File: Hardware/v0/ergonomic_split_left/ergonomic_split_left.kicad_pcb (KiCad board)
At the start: 2 copper layers, 182.6 x 172.4 mm, 96 parts, among them J1 USB_C_Receptacle_USB2.0, J2 Right_Interface, J3 Conn_01x02_Male, J5 Conn_02x03_Odd_Even, SW1 SW_Push, SW10 L31, SW11 L41, SW12 L51, SW13 L02, SW14 L12, SW15 L22, SW16 L32, SW17 L42, SW18 L52, SW19 L03, SW2 L00, SW20 L13, SW21 L23, SW22 L33, SW23 L43, SW24 L53, SW25 L04, SW26 L14, SW27 L24, SW28 L34, SW29 L44, SW3 L10, SW30 L54, SW31 L05, SW32 L15, SW33 L25, SW34 L35, SW35 L55, SW36 L16, SW37 L36, SW38 L56, SW39 L06, SW4 L20, SW40 L_Encoder, SW5 L30, SW6 L40, SW7 L01, SW8 L11, SW9 L21, U1 SRV05-4, U2 PCAL9555AHF, U6 ATmega32U4-AU, U9 TCR2EF33, X2 KC2016K

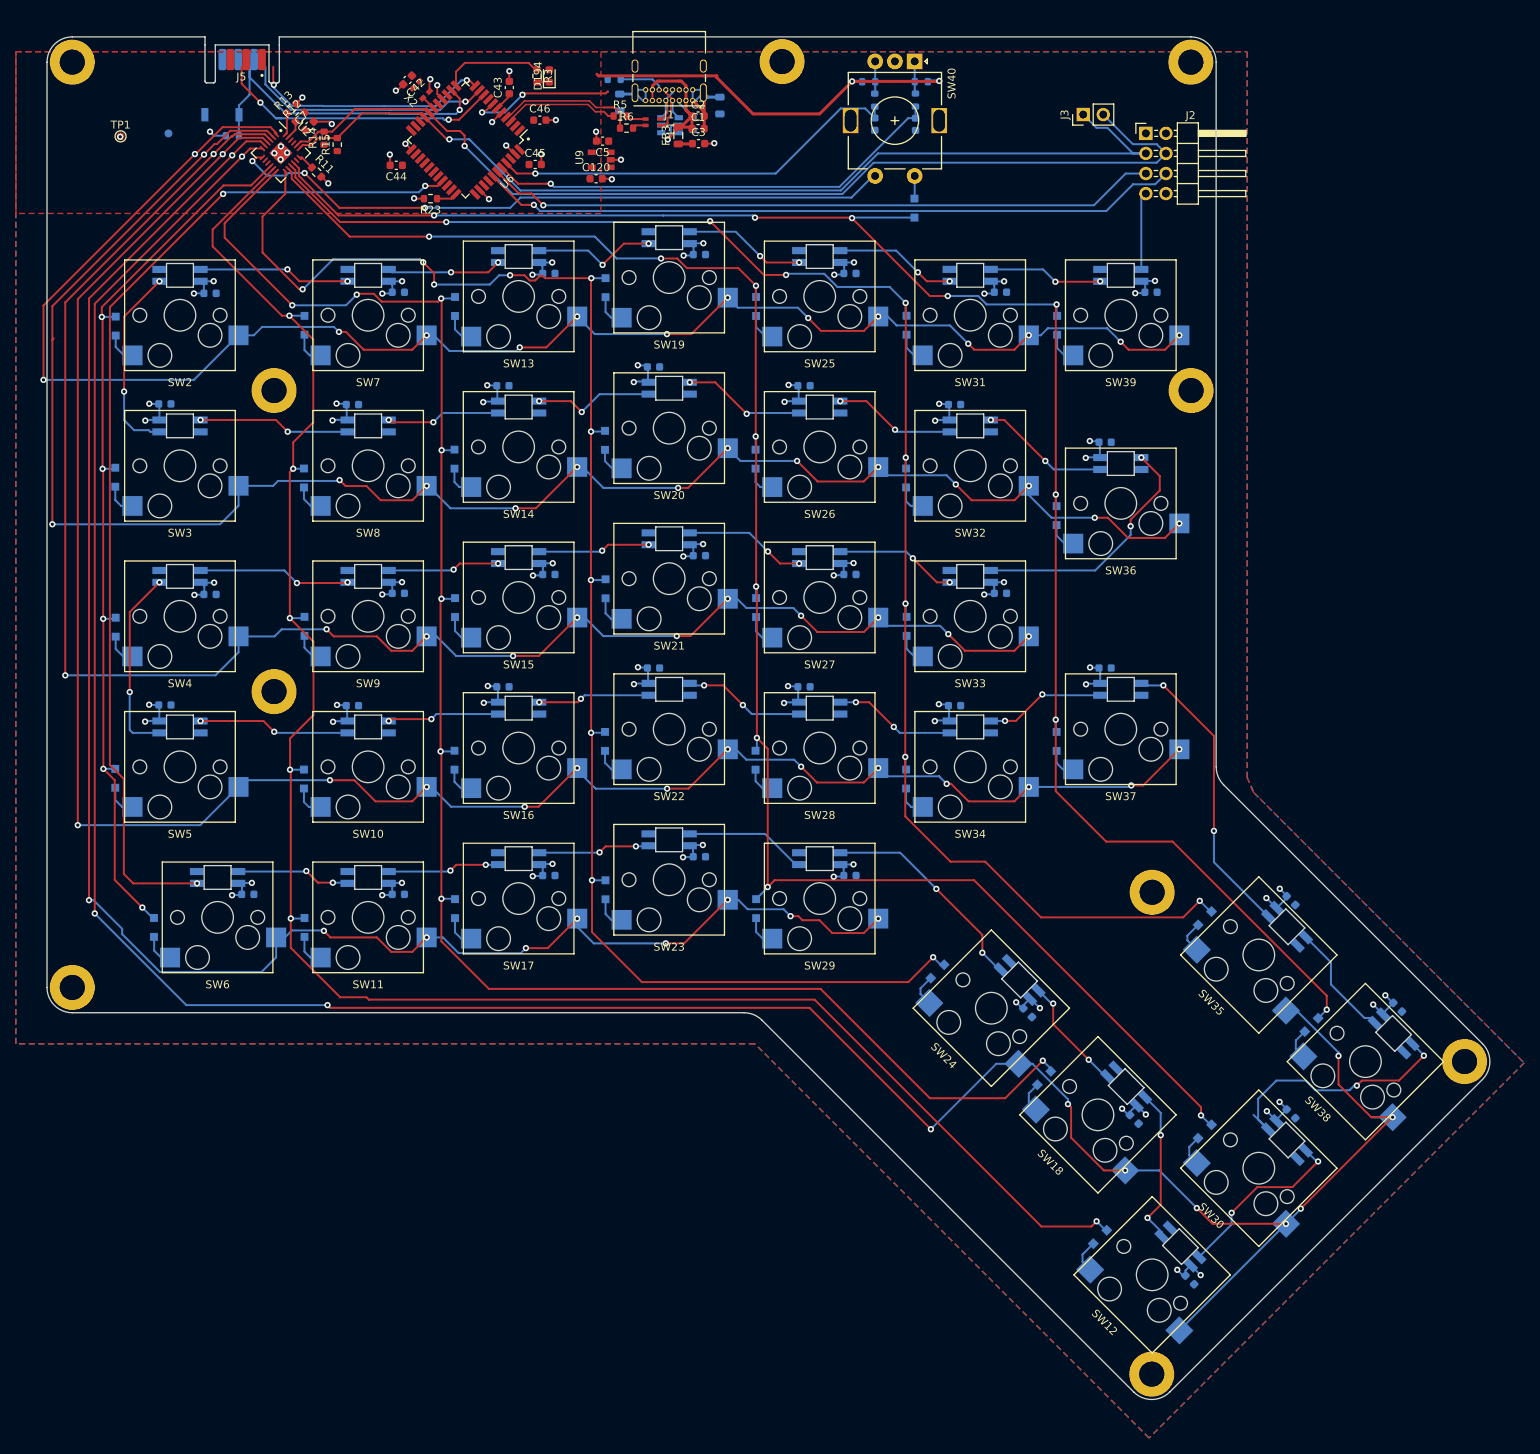
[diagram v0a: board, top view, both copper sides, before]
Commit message: Fixing power planes and connector positions
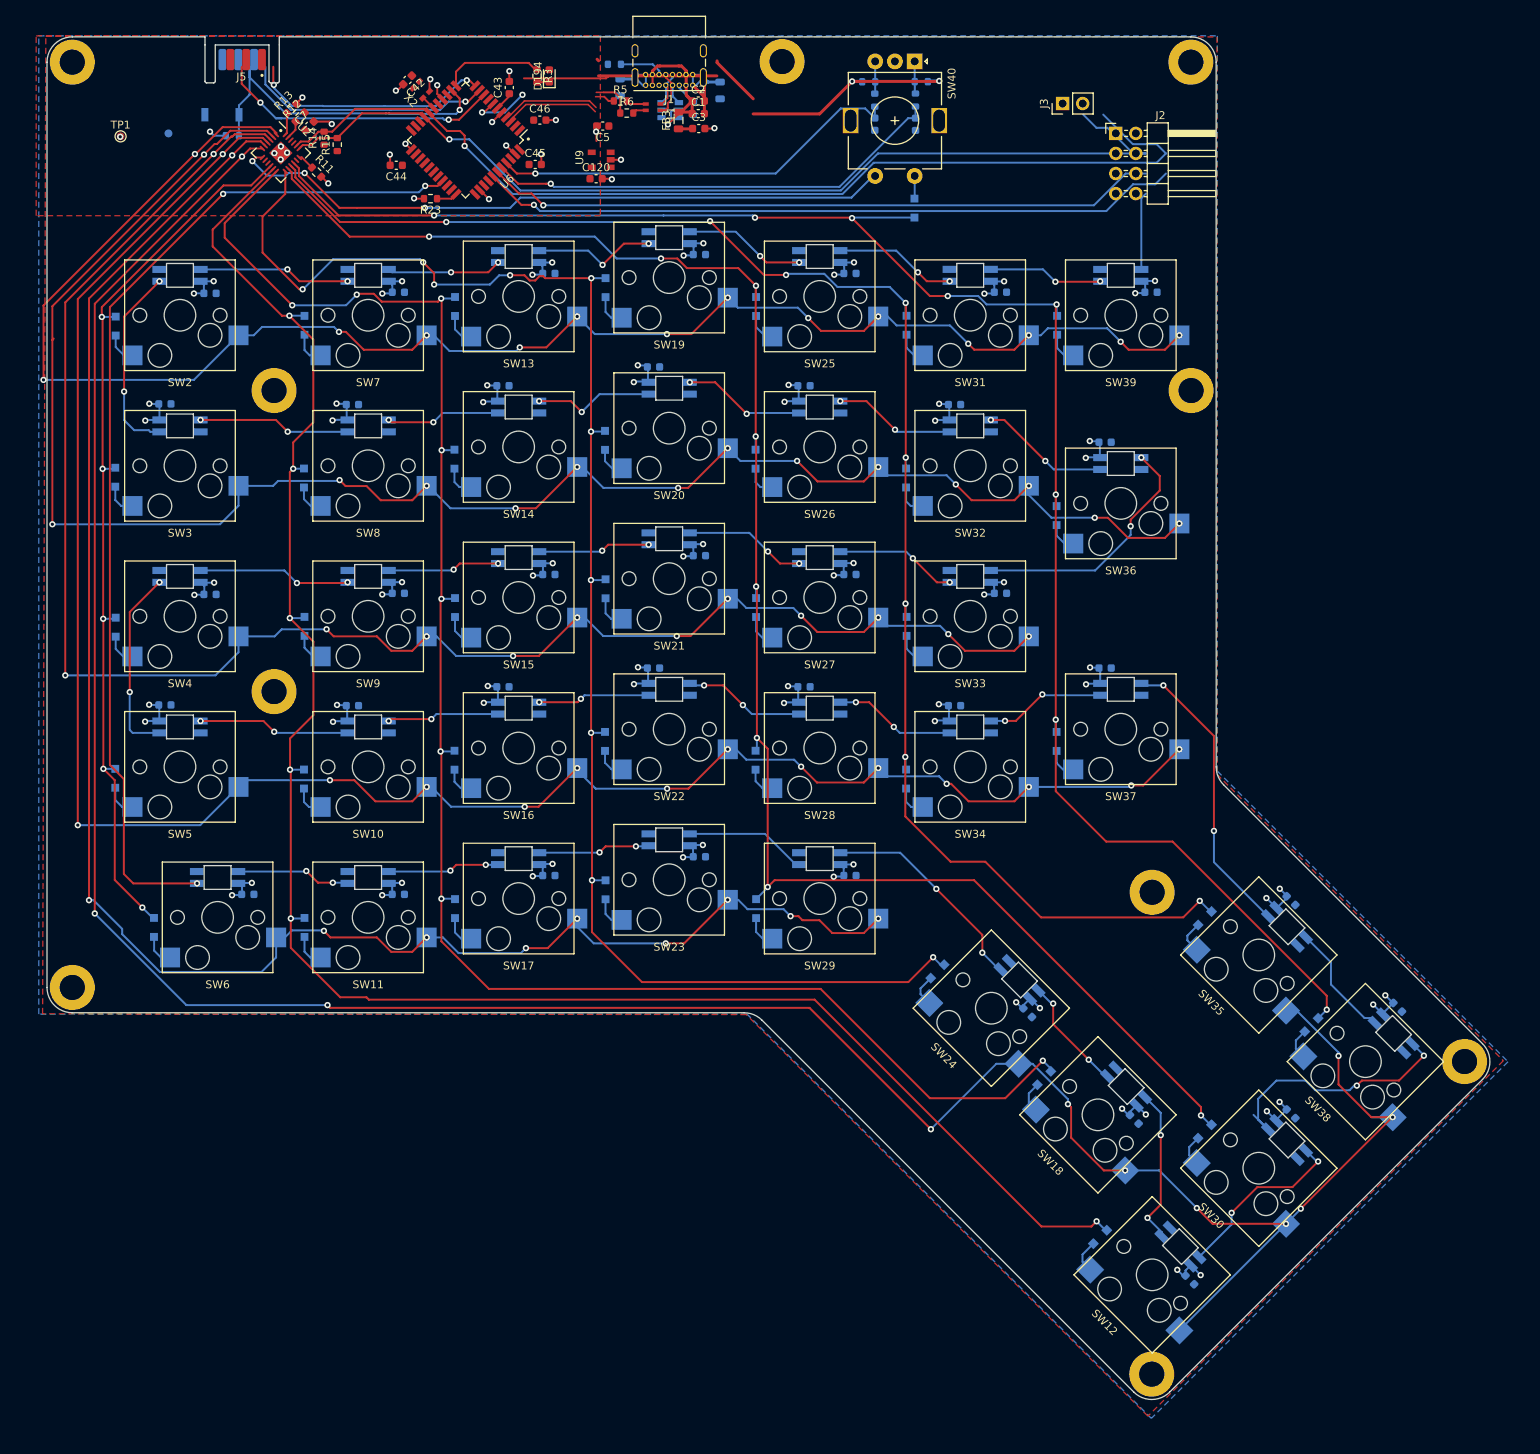
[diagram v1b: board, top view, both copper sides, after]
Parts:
- moved J2 3.81 mm to (212.1, 65.9)
- moved J3 2.95 mm to (205.4, 62.1)
- moved J1 1.93 mm to (158.5, 59.8)
- moved C1 1.91 mm to (159.3, 63.4)
- moved L1 1.91 mm to (153.5, 62.6)
- moved C5 1.91 mm to (147.2, 65.0)
- moved FB3 1.91 mm to (156.8, 64.2)
- moved R1 1.91 mm to (148.6, 57.1)
- moved R6 1.91 mm to (150.2, 63.3)
- moved C3 1.91 mm to (159.3, 65.3)
- moved FB1 1.91 mm to (162.0, 60.5)
- moved FB2 1.91 mm to (149.3, 60.1)
- moved R5 1.91 mm to (149.4, 61.8)
- moved U1 1.91 mm to (155.7, 62.9)
- moved C2 1.91 mm to (159.3, 61.8)
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
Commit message: Cleaning up routing
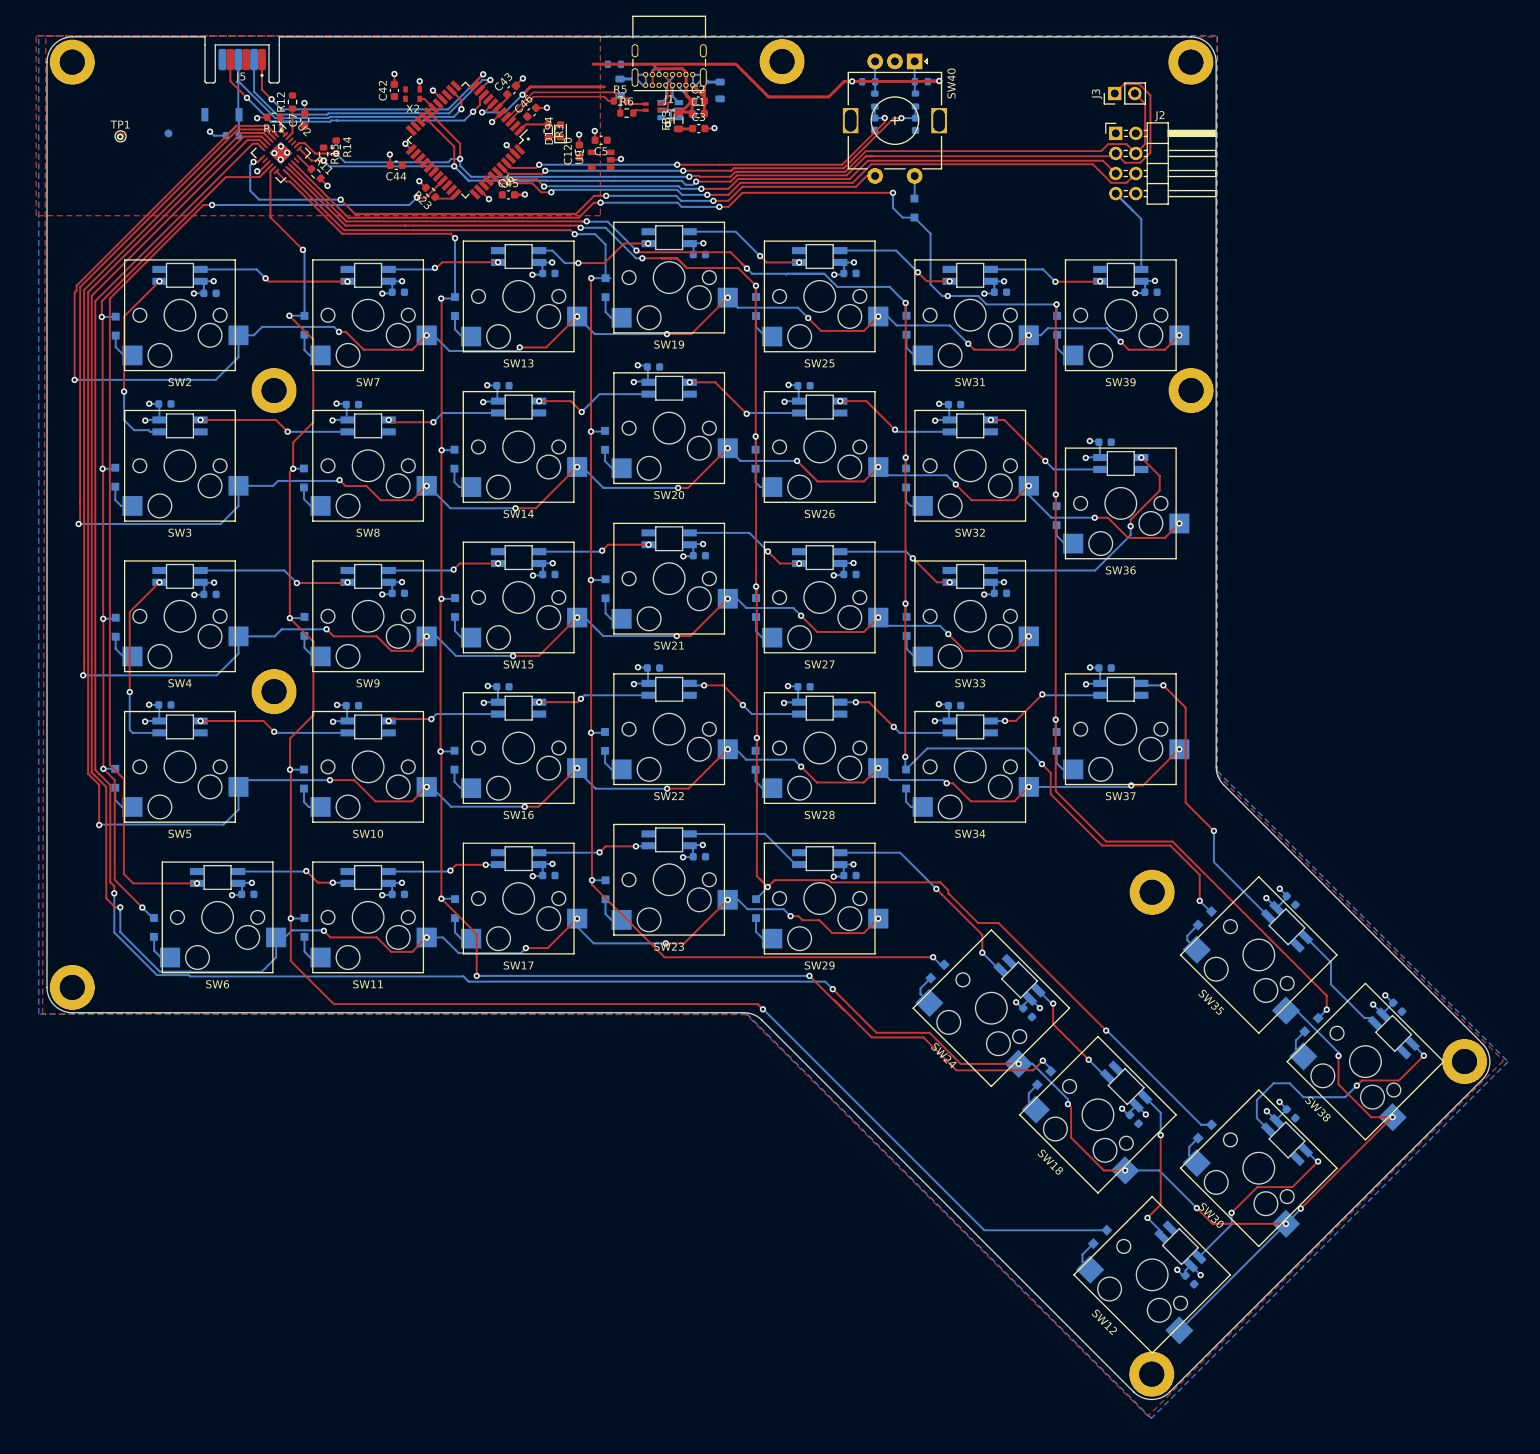
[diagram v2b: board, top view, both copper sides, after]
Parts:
- moved D194 7.10 mm to (141.8, 65.6)
- moved R3 7.10 mm to (140.3, 65.6)
- moved J3 6.73 mm to (212.0, 60.8)
- moved C45 5.12 mm to (135.2, 73.7)
- moved C120 4.09 mm to (144.2, 68.1), turned to 90 degrees
- moved R13 2.50 mm to (105.6, 63.9), turned to 180 degrees
- moved R12 2.13 mm to (107.9, 61.9), turned to 90 degrees
- moved C42 2.12 mm to (120.8, 60.5), turned to 90 degrees
- moved R15 2.11 mm to (111.8, 68.5), turned to 270 degrees
- moved R14 1.90 mm to (113.4, 67.6), turned to 270 degrees
- moved C5 1.81 mm to (147.0, 66.8)
- moved C46 1.44 mm to (138.2, 63.2), turned to 45 degrees
- moved X2 1.21 mm to (123.1, 60.9), turned to 180 degrees
- moved C7 0.96 mm to (109.4, 64.2), turned to 90 degrees
- moved R23 0.79 mm to (125.4, 73.4), turned to 135 degrees
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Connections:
- U6 pad 1: Net-(U6-Pad1) -> /uController/nCAPS_LED
- U6 pad 12: /uController/nCAPS_LED -> Net-(U6-Pad12)
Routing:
- net /IO Expander/COL[3]: track 200.6 -> 183.9 mm, vias 10 -> 7
- net /IO Expander/SDA: track 124.9 -> 137.5 mm, vias 1 -> 3
- net /IO Expander/COL[2]: track 221.5 -> 210.7 mm, vias 8 -> 9
- net /IO Expander/ROW[5]: track 345.4 -> 336.4 mm, vias 11 -> 10
- net /uController/nCAPS_LED: track 12.9 -> 3.94 mm
- net /uController/MOSI: track 31.7 -> 38.9 mm
- net /IO Expander/COL[5]: track 202.6 -> 208.9 mm, vias 8 -> 9
- net /uController/MISO: track 30.8 -> 36.6 mm
- net /IO Expander/COL[1]: track 238.7 -> 233.4 mm, vias 6 -> 7
- net /IO Expander/ROW[1]: track 229.3 -> 224.0 mm, vias 14 -> 13
- net /IO Expander/COL[4]: track 220.9 -> 225.4 mm
- net /uController/SCK: track 36.8 -> 41.1 mm
- net /Right Interface/ENCODER_A_R: track 85.5 -> 81.3 mm, vias 1 -> 2
- net /IO Expander/ROW[6]: track 84.5 -> 88.7 mm, vias 3 -> 4
- net /Right Interface/RGB_DIN: track 9.83 -> 14.0 mm
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
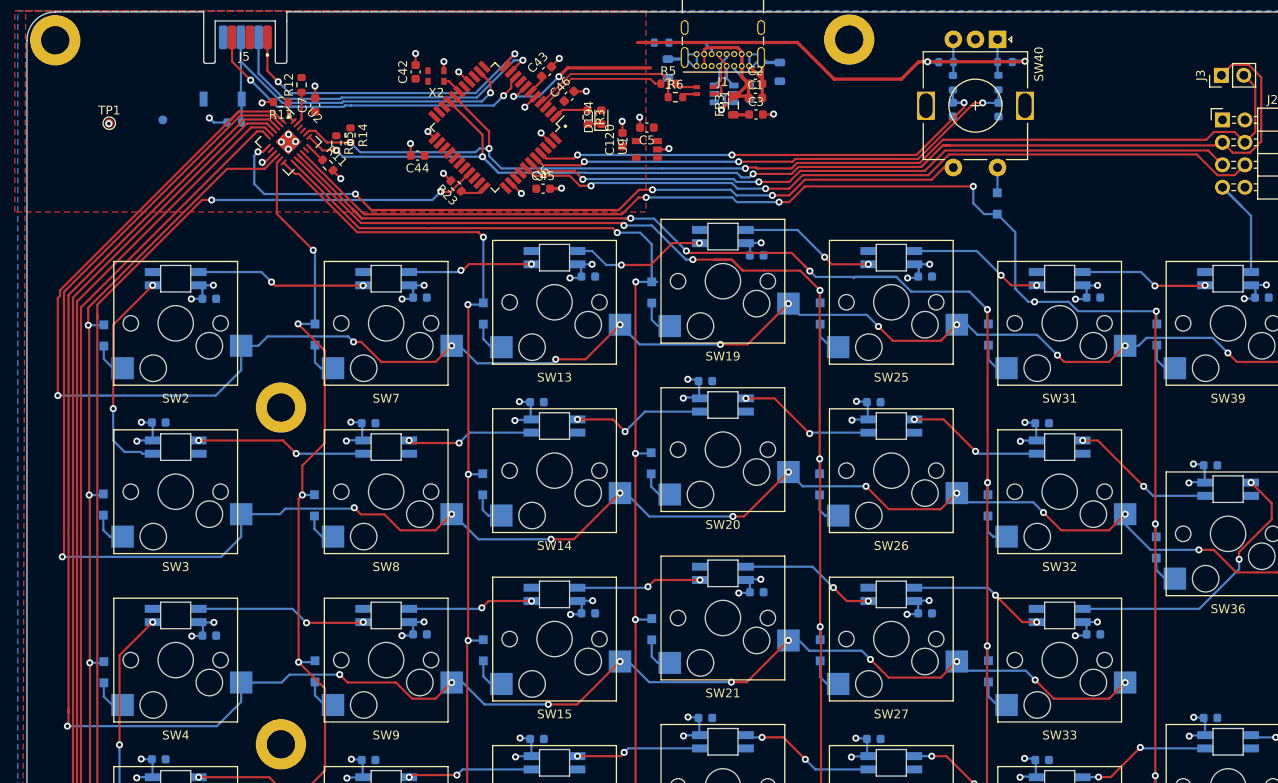
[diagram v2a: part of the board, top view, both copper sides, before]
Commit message: Passes DRC Fixed component clashes Fixed traces blocking 5V0 power plane
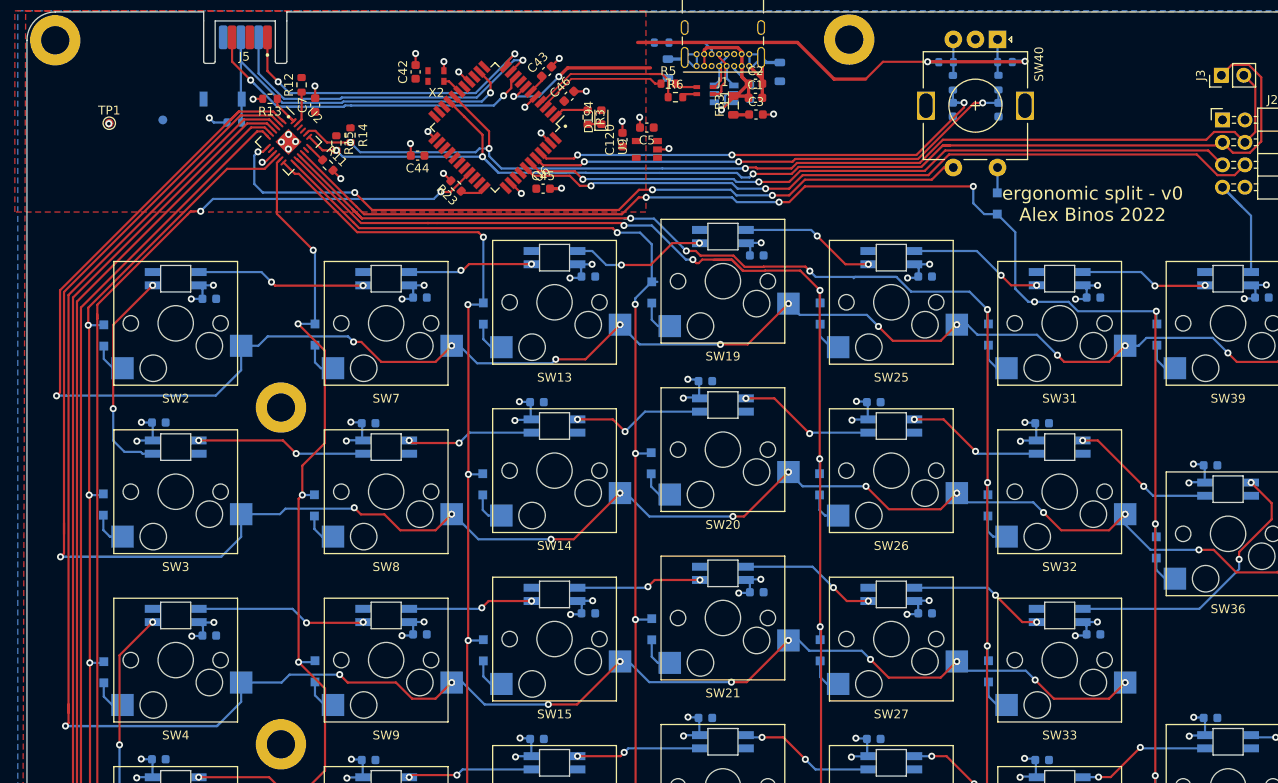
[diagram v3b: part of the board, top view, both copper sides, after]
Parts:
- moved R13 1.27 mm to (104.3, 63.5)
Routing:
- net /IO Expander/ROW[1]: track 224.0 -> 243.4 mm
- net /IO Expander/ROW[2]: track 217.9 -> 236.3 mm
- net Net-(R13-Pad1): track 2.71 -> 4.45 mm
- net /IO Expander/COL[3]: track 183.9 -> 182.8 mm
- net /IO Expander/COL[5]: track 208.9 -> 207.9 mm
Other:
- board text added: "ergonomic split - v0 Alex Binos 2022"
